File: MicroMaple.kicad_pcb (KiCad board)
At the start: 2 copper layers, 38.1 x 38.1 mm, 40 parts, among them P1 USB_OTG, P2 CONN_01X14, P3 CONN_01X14, P4 CONN_01X12, Q1 8050, Q2 8050, SW1 USR_BUT, SW2 RST_BUTTON, U1 STM32F103C8T6, U2 XC6206P332MR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

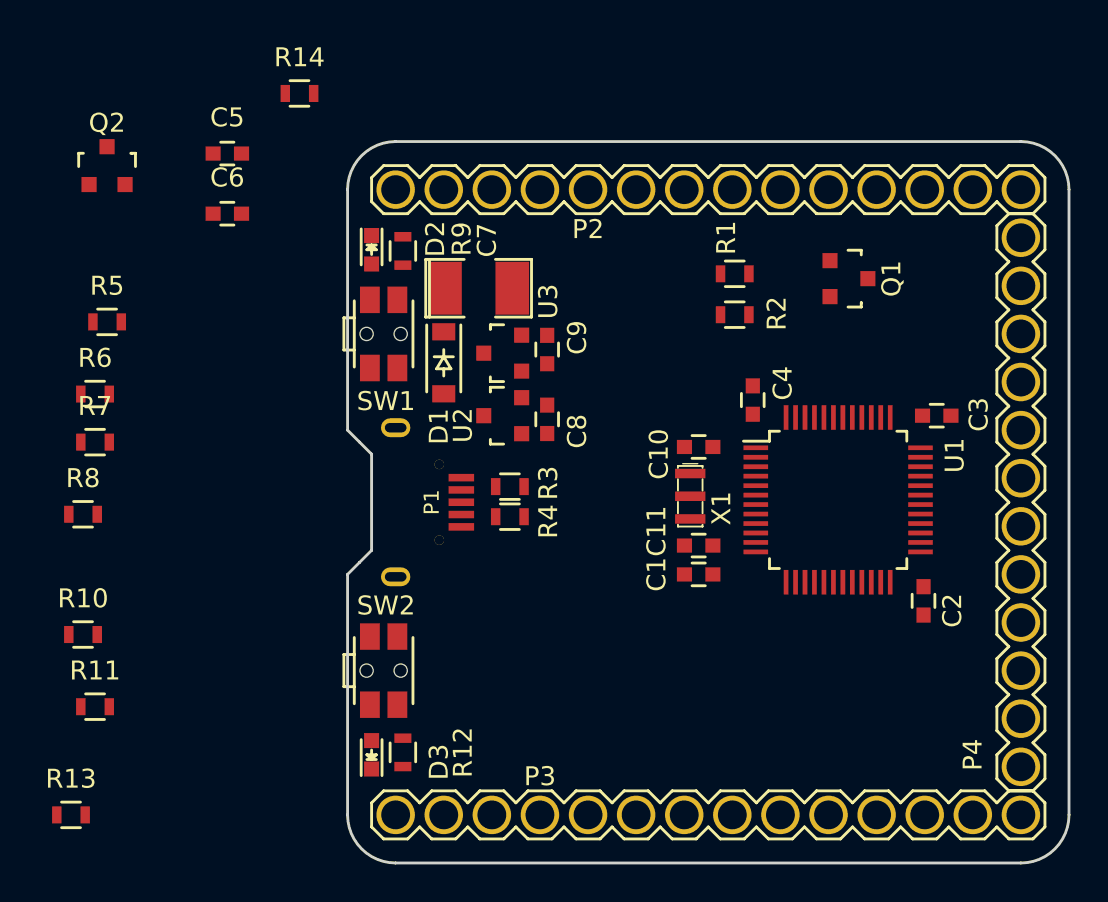
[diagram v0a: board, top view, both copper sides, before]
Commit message: finish the PCB layout and track
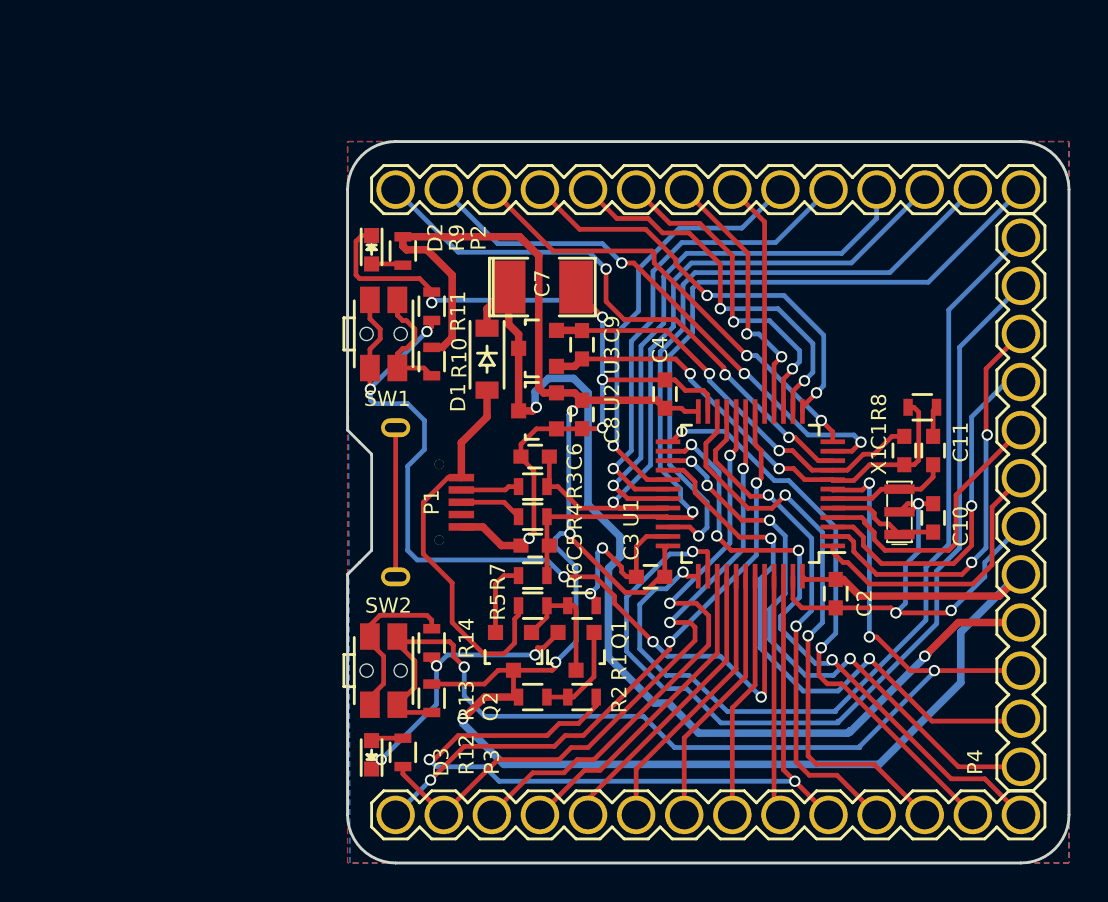
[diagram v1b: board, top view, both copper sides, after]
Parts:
- moved R8 44.7 mm to (159.9, 105.5), turned to 180 degrees
- moved Q2 33.4 mm to (138.3, 118.4), turned to 180 degrees
- moved R14 29.8 mm to (134.0, 117.9), turned to 270 degrees
- moved R6 28.0 mm to (141.9, 116.0), turned to 180 degrees
- moved R11 27.6 mm to (134.0, 100.1), turned to 270 degrees
- moved R5 27.0 mm to (139.3, 116.0), turned to 180 degrees
- moved C5 26.3 mm to (139.4, 112.8), turned to 180 degrees
- moved Q1 24.4 mm to (141.6, 118.4), turned to 180 degrees
- moved R7 24.2 mm to (139.3, 114.4), turned to 180 degrees
- moved R1 23.8 mm to (141.9, 120.8)
- moved R10 23.4 mm to (134.0, 103.1), turned to 270 degrees
- moved R2 22.8 mm to (139.3, 120.8), turned to 180 degrees
- moved C6 20.7 mm to (139.4, 108.1), turned to 180 degrees
- moved R13 20.0 mm to (134.0, 120.8), turned to 90 degrees
- moved C3 17.3 mm to (145.5, 114.4), turned to 180 degrees
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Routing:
- net VCC: track 0.00 -> 117.2 mm, vias 0 -> 4
- net GND: track 0.00 -> 97.9 mm, vias 0 -> 13
- net /PB8: track 0.00 -> 62.6 mm, vias 0 -> 5
- net /RST: track 0.00 -> 59.2 mm, vias 0 -> 4
- net +BATT: track 0.00 -> 56.1 mm, vias 0 -> 2
- net /PA15: track 0.00 -> 49.4 mm, vias 0 -> 1
- net /PA14: track 0.00 -> 47.0 mm, vias 0 -> 1
- net /PB9: track 0.00 -> 44.1 mm, vias 0 -> 2
- net /PA12: track 0.00 -> 42.0 mm, vias 0 -> 1
- net /PA11: track 0.00 -> 39.8 mm, vias 0 -> 1
- net /PB1: track 0.00 -> 35.9 mm, vias 0 -> 2
- net /PA13: track 0.00 -> 35.9 mm, vias 0 -> 1
- net /PB13: track 0.00 -> 33.2 mm, vias 0 -> 4
- net /PB0: track 0.00 -> 32.8 mm, vias 0 -> 3
- net /PB11: track 0.00 -> 30.9 mm, vias 0 -> 2
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- added copper zone on B.Cu, net GND
- added copper zone on F.Cu, net GND
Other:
- net class Power added: clearance 0.2, trace_width 0.4, via_dia 0.6, via_drill 0.4

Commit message: finish the PCB design
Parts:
- added P5: CONN_01X01, myFootprints:Debug_Pin_1, F.Cu at (157.5, 100.3)
- added P6: CONN_01X01, myFootprints:Debug_Pin_1, F.Cu at (161.3, 100.3)
- added P7: CONN_01X01, myFootprints:Debug_Pin_1, F.Cu at (162.4, 117.0)
- added P8: CONN_01X01, myFootprints:Debug_Pin_1, F.Cu at (159.8, 116.9)
- moved P4 0.06 mm to (165.1, 110.4)
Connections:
- P4 pad 10: /RST -> +5V
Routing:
- net +5V: track 21.0 -> 69.3 mm, vias 0 -> 1
- net GND: track 97.9 -> 81.7 mm, vias 13 -> 11
- net /RST: track 59.2 -> 49.0 mm
- net VCC: track 117.2 -> 109.4 mm
- net /PB9: track 44.1 -> 46.7 mm, vias 2 -> 1
- net /PA13: track 35.9 -> 37.1 mm
- net /PA14: track 47.0 -> 47.9 mm
- net /PA15: track 49.4 -> 50.0 mm
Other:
- board text added: "+5V"
- board text added: "GND"
- board text added: "PA0/PWM/ADC"
- board text added: "PA1/PWM/ADC"
- board text added: "PA10/PWM/RX1"
- board text added: "PA11/USB_DM"
- board text added: "PA12/USB_DP"
- board text added: "PA13"
- board text added: "PA14"
- board text added: "PA15"
- board text added: "PA2/PWM/ADC/TX2"
- board text added: "PA3/PWM/ADC/RX2"
- board text added: "PA4/ADC/NSS1"
- board text added: "PA5/ADC/SCK1"
- board text added: "PA6/PWM/ADC/MISO1"
- board text added: "PA7/PWM/ADC/MOSI1"
- board text added: "PA8/PWM"
- board text added: "PA9/PWM/TX1"
- board text added: "PB0/PWM/ADC"
- board text added: "PB1"
- board text added: "PB10/TX3/SCL2"
- board text added: "PB11/RX3/SDA2"
- board text added: "PB12/NSS2"
- board text added: "PB13/SCK2"
- board text added: "PB14/MISO2"
- board text added: "PB15 MISO2"
- board text added: "PB2"
- board text added: "PB3"
- board text added: "PB4"
- board text added: "PB5"
- board text added: "PB6/PWM/SDA1"
- board text added: "PB7/PWM/SCL1"
- board text added: "PB8"
- board text added: "PB9"
- board text added: "PC13"
- board text added: "PC14"
- board text added: "PC15"
- board text added: "Reset"
- board text added: "SWCLK"
- board text added: "SWDIO"
- board text added: "VBAT"
- board text added: "VCC"
- board text added: "VIN"
- board text added: "boot0"

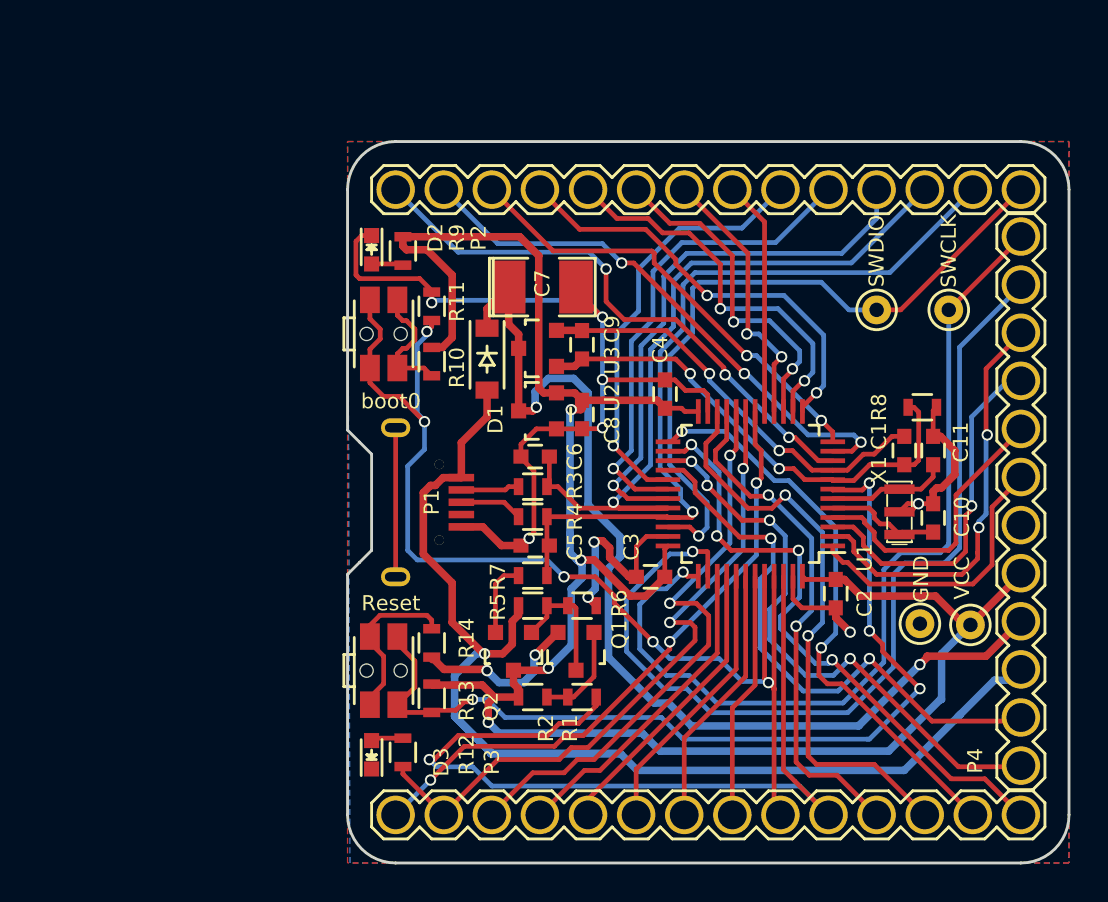
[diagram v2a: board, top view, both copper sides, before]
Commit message: optimize the layout and tracks, then add the logo and some text
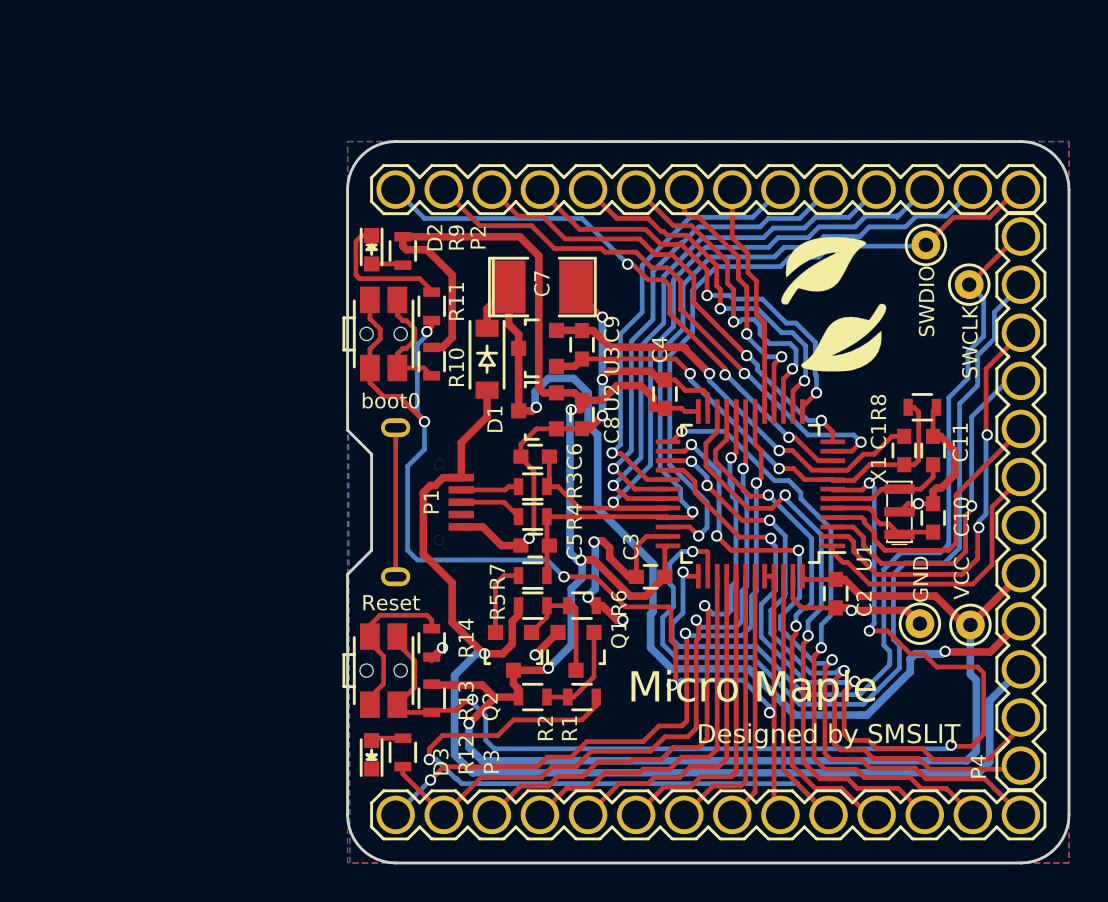
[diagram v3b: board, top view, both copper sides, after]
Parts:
- added G***: LOGO, myFootprints:logo, F.Cu at (155.2, 100.0)
- moved P5 4.31 mm to (160.1, 96.9)
- moved P6 1.72 mm to (162.4, 99.0)
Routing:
- net GND: track 81.7 -> 70.3 mm
- net /RST: track 49.0 -> 58.9 mm
- net VCC: track 109.4 -> 116.0 mm
- net /PB15: track 30.3 -> 36.5 mm
- net +5V: track 69.3 -> 63.4 mm
- net /PB0: track 32.8 -> 37.6 mm
- net /PB13: track 33.2 -> 36.6 mm
- net /PB4: track 15.6 -> 19.0 mm
- net /PB1: track 35.9 -> 39.1 mm
- net /PB3: track 17.0 -> 19.9 mm
- net /PA15: track 50.0 -> 47.1 mm
- net /PB12: track 30.5 -> 33.4 mm
- net /PB14: track 30.7 -> 33.0 mm
- net /PB2: track 30.9 -> 33.1 mm
- net /PA14: track 47.9 -> 45.8 mm
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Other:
- board text added: "Designed by SMSLIT"
- board text added: "Micro Maple"
